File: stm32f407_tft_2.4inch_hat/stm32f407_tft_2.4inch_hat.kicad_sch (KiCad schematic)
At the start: 3 parts, among them P1 Conn_02x25_Row_Letter_First_S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, P2 Conn_02x25_Row_Letter_First_S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, U1 CR2013-MI2120

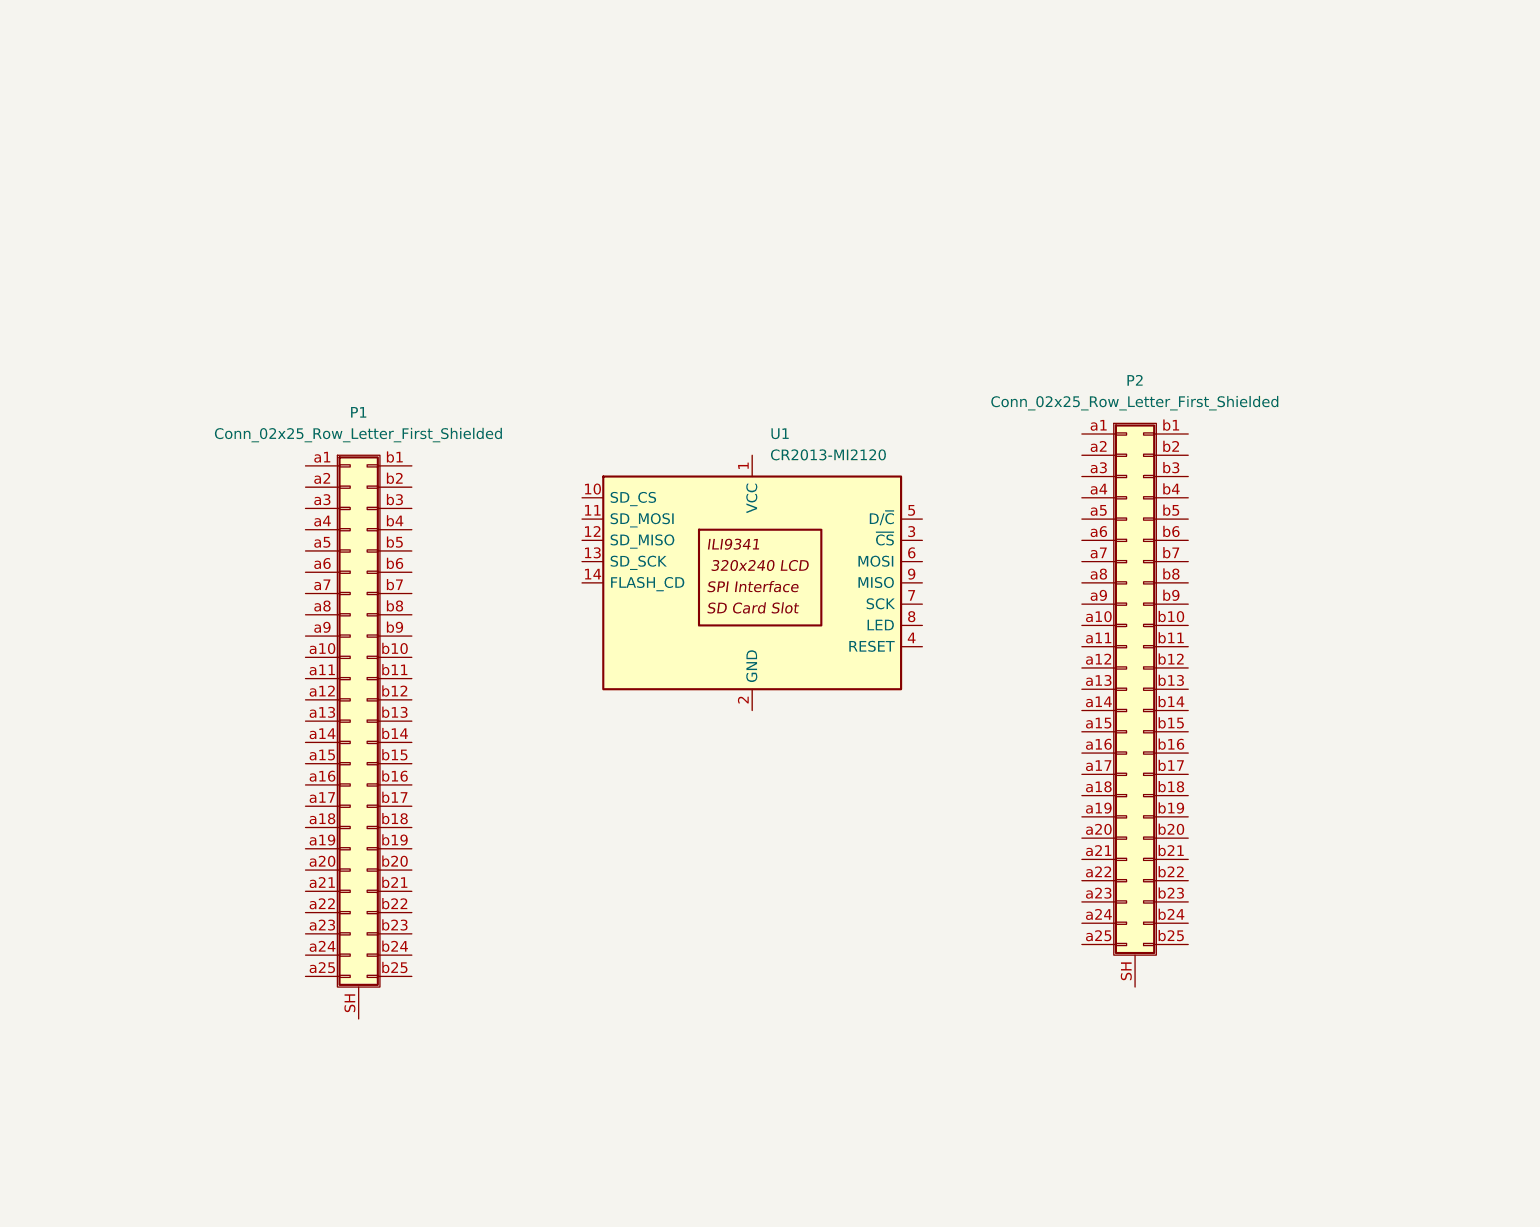
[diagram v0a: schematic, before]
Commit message: Add 3 connector for i2c & uart
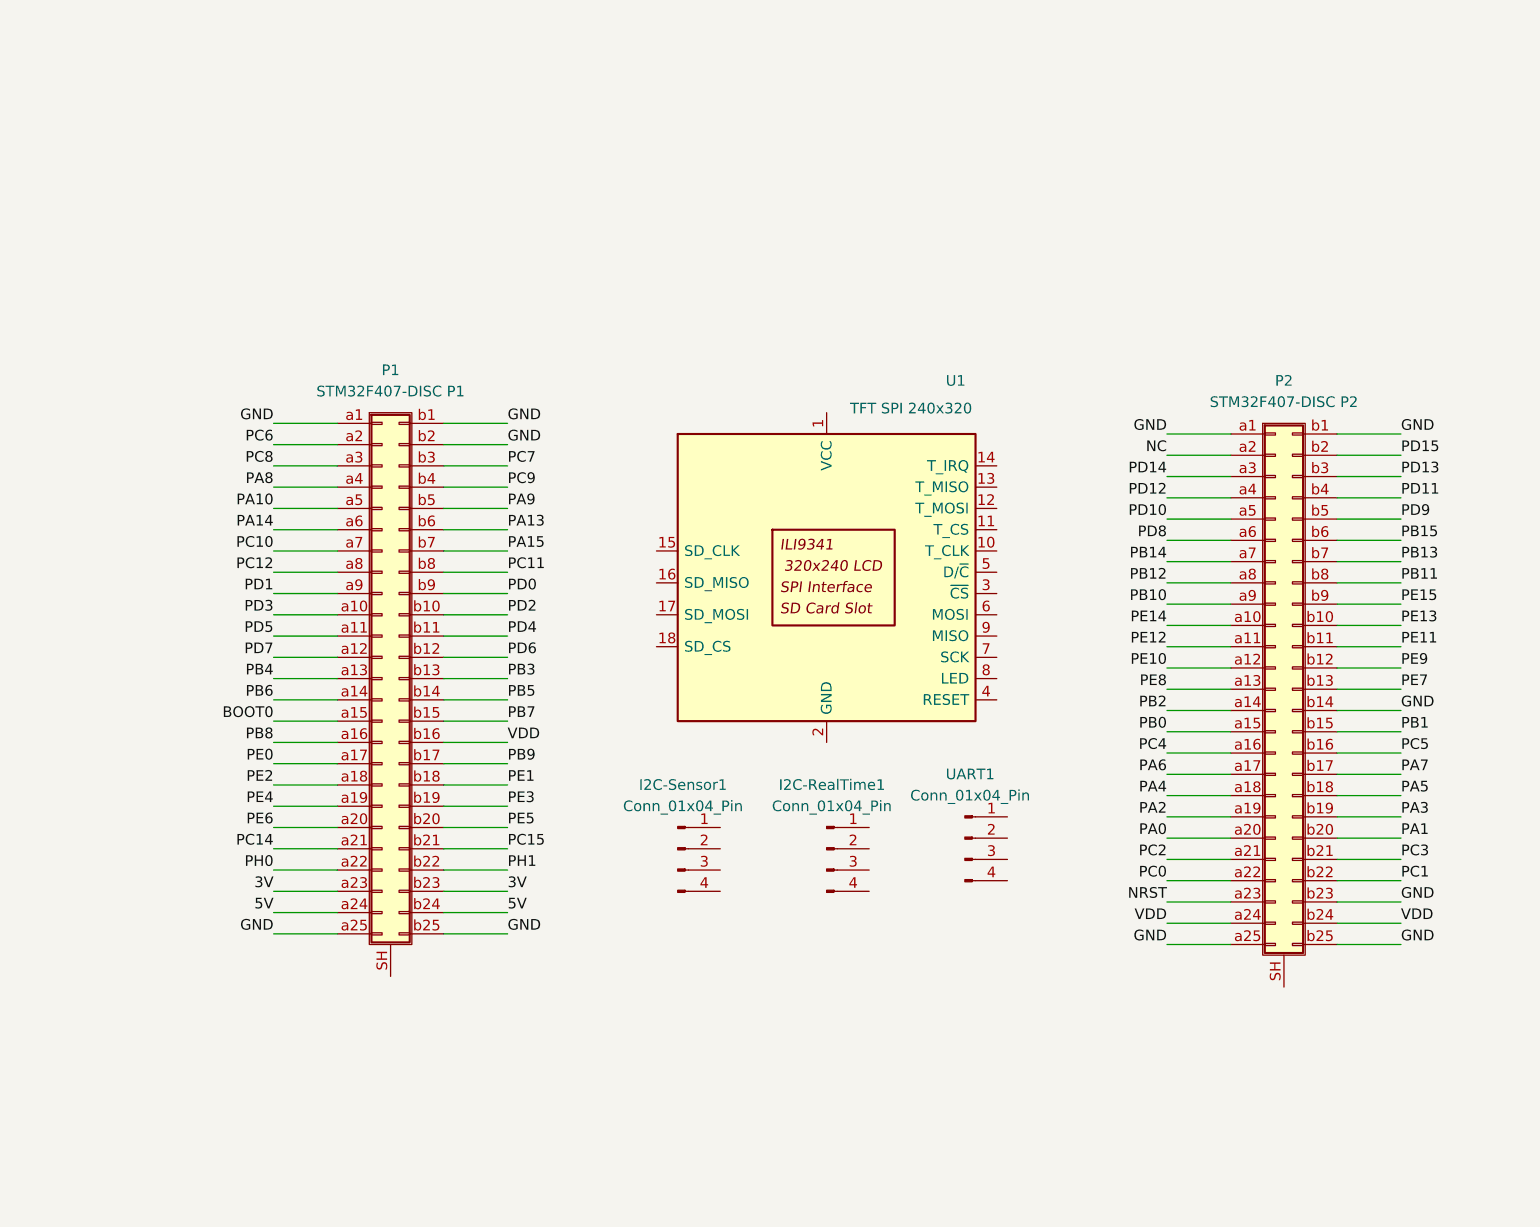
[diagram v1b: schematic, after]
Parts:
- added I2C-RealTime1, I2C-Sensor1, UART1: Conn_01x04_Pin, Connector_PinHeader_2.54mm:PinHeader_1x04_P2.54mm_Horizontal, symbol Connector:Conn_01x04_Pin
- P1: value Conn_02x25_Row_Letter_First_Shielded -> STM32F407-DISC P1; symbol Connector_Generic_Shielded:Conn_02x25_Row_Letter_First_Shielded -> stm32f407_tft_hat:Conn_Discovery_P1_2x25
- P2: value Conn_02x25_Row_Letter_First_Shielded -> STM32F407-DISC P2; symbol Connector_Generic_Shielded:Conn_02x25_Row_Letter_First_Shielded -> stm32f407_tft_hat:Conn_Discovery_P2_2x25
- U1: value CR2013-MI2120 -> TFT SPI 240x320
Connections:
- net GND: now reaches P1.a1 (GND)
- net GND: now also P1.a25 (GND), P1.b1 (GND), P1.b2 (5V), P1.b25 (GND), P2.a1 (GND), P2.a25 (GND), P2.b1 (GND), P2.b14 (PE9), P2.b23 (PD13), P2.b25 (GND)
- net PD3: now reaches P1.a10 (PB8)
- net PD5: now reaches P1.a11 (BOOT0)
- net PD7: now reaches P1.a12 (PB6)
- net PB4: now reaches P1.a13 (PB4)
- net PB6: now reaches P1.a14 (PD7)
- net BOOT0: now reaches P1.a15 (PD5)
- net PB8: now reaches P1.a16 (PD3)
- net PE0: now reaches P1.a17 (PD1)
- net PE2: now reaches P1.a18 (PC12)
- net PE4: now reaches P1.a19 (PC10)
- net PC6: now reaches P1.a2 (5V)
- net PE6: now reaches P1.a20 (PA14)
- net PC14: now reaches P1.a21 (PA10)
- net PH0: now reaches P1.a22 (PA8)
- net 3V: now reaches P1.a23 (PC8)
- net 3V: now also P1.b23 (PC7)
- net 5V: now reaches P1.a24 (PC6)
- net 5V: now also P1.b24 (GND)
- net PC8: now reaches P1.a3 (3V)
- net PA8: now reaches P1.a4 (PH0)
- net PA10: now reaches P1.a5 (PC14)
- net PA14: now reaches P1.a6 (PE6)
- net PC10: now reaches P1.a7 (PE4)
- net PC12: now reaches P1.a8 (PE2)
- net PD1: now reaches P1.a9 (PE0)
- net PD2: now reaches P1.b10 (VDD)
- net PD4: now reaches P1.b11 (PB7)
- net PD6: now reaches P1.b12 (PB5)
- net PB3: now reaches P1.b13 (PB3)
- net PB5: now reaches P1.b14 (PD6)
- net PB7: now reaches P1.b15 (PD4)
- net VDD: now reaches P1.b16 (PD2)
- net VDD: now also P2.a24 (NC), P2.b24 (PD15)
- net PB9: now reaches P1.b17 (PD0)
- net PE1: now reaches P1.b18 (PC11)
- net PE3: now reaches P1.b19 (PA15)
- net PE5: now reaches P1.b20 (PA13)
- net PC15: now reaches P1.b21 (PA9)
- net PH1: now reaches P1.b22 (PC9)
- net PC7: now reaches P1.b3 (3V)
- net PC9: now reaches P1.b4 (PH1)
- net PA9: now reaches P1.b5 (PC15)
- net PA13: now reaches P1.b6 (PE5)
- net PA15: now reaches P1.b7 (PE3)
- net PC11: now reaches P1.b8 (PE1)
- net PD0: now reaches P1.b9 (PB9)
- net PE14: now reaches P2.a10 (PC4)
- net PE12: now reaches P2.a11 (PB0)
- net PE10: now reaches P2.a12 (PB2)
- net PE8: now reaches P2.a13 (PE8)
- net PB2: now reaches P2.a14 (PE10)
- net PB0: now reaches P2.a15 (PE12)
- net PC4: now reaches P2.a16 (PE14)
- net PA6: now reaches P2.a17 (PB10)
- net PA4: now reaches P2.a18 (PB12)
- net PA2: now reaches P2.a19 (PB14)
- net NC: now reaches P2.a2 (VDD)
- net PA0: now reaches P2.a20 (PD8)
- net PC2: now reaches P2.a21 (PD10)
- net PC0: now reaches P2.a22 (PD12)
- net NRST: now reaches P2.a23 (PD14)
- net PD14: now reaches P2.a3 (NRST)
- net PD12: now reaches P2.a4 (PC0)
- net PD10: now reaches P2.a5 (PC2)
- net PD8: now reaches P2.a6 (PA0)
- net PB14: now reaches P2.a7 (PA2)
- net PB12: now reaches P2.a8 (PA4)
- net PB10: now reaches P2.a9 (PA6)
- net PE13: now reaches P2.b10 (PC5)
- net PE11: now reaches P2.b11 (PB1)
- net PE9: now reaches P2.b12 (GND)
- net PE7: now reaches P2.b13 (PE7)
- net PB1: now reaches P2.b15 (PE11)
- net PC5: now reaches P2.b16 (PE13)
- net PA7: now reaches P2.b17 (PE15)
- net PA5: now reaches P2.b18 (PB11)
- net PA3: now reaches P2.b19 (PB13)
- net PD15: now reaches P2.b2 (VDD)
- net PA1: now reaches P2.b20 (PB15)
- net PC3: now reaches P2.b21 (PD9)
- net PC1: now reaches P2.b22 (PD11)
- net PD13: now reaches P2.b3 (GND)
- net PD11: now reaches P2.b4 (PC1)
- net PD9: now reaches P2.b5 (PC3)
- net PB15: now reaches P2.b6 (PA1)
- net PB13: now reaches P2.b7 (PA3)
- net PB11: now reaches P2.b8 (PA5)
- net PE15: now reaches P2.b9 (PA7)
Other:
- moved on the sheet: P1, P2

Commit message: Update sch pin j1 & j2
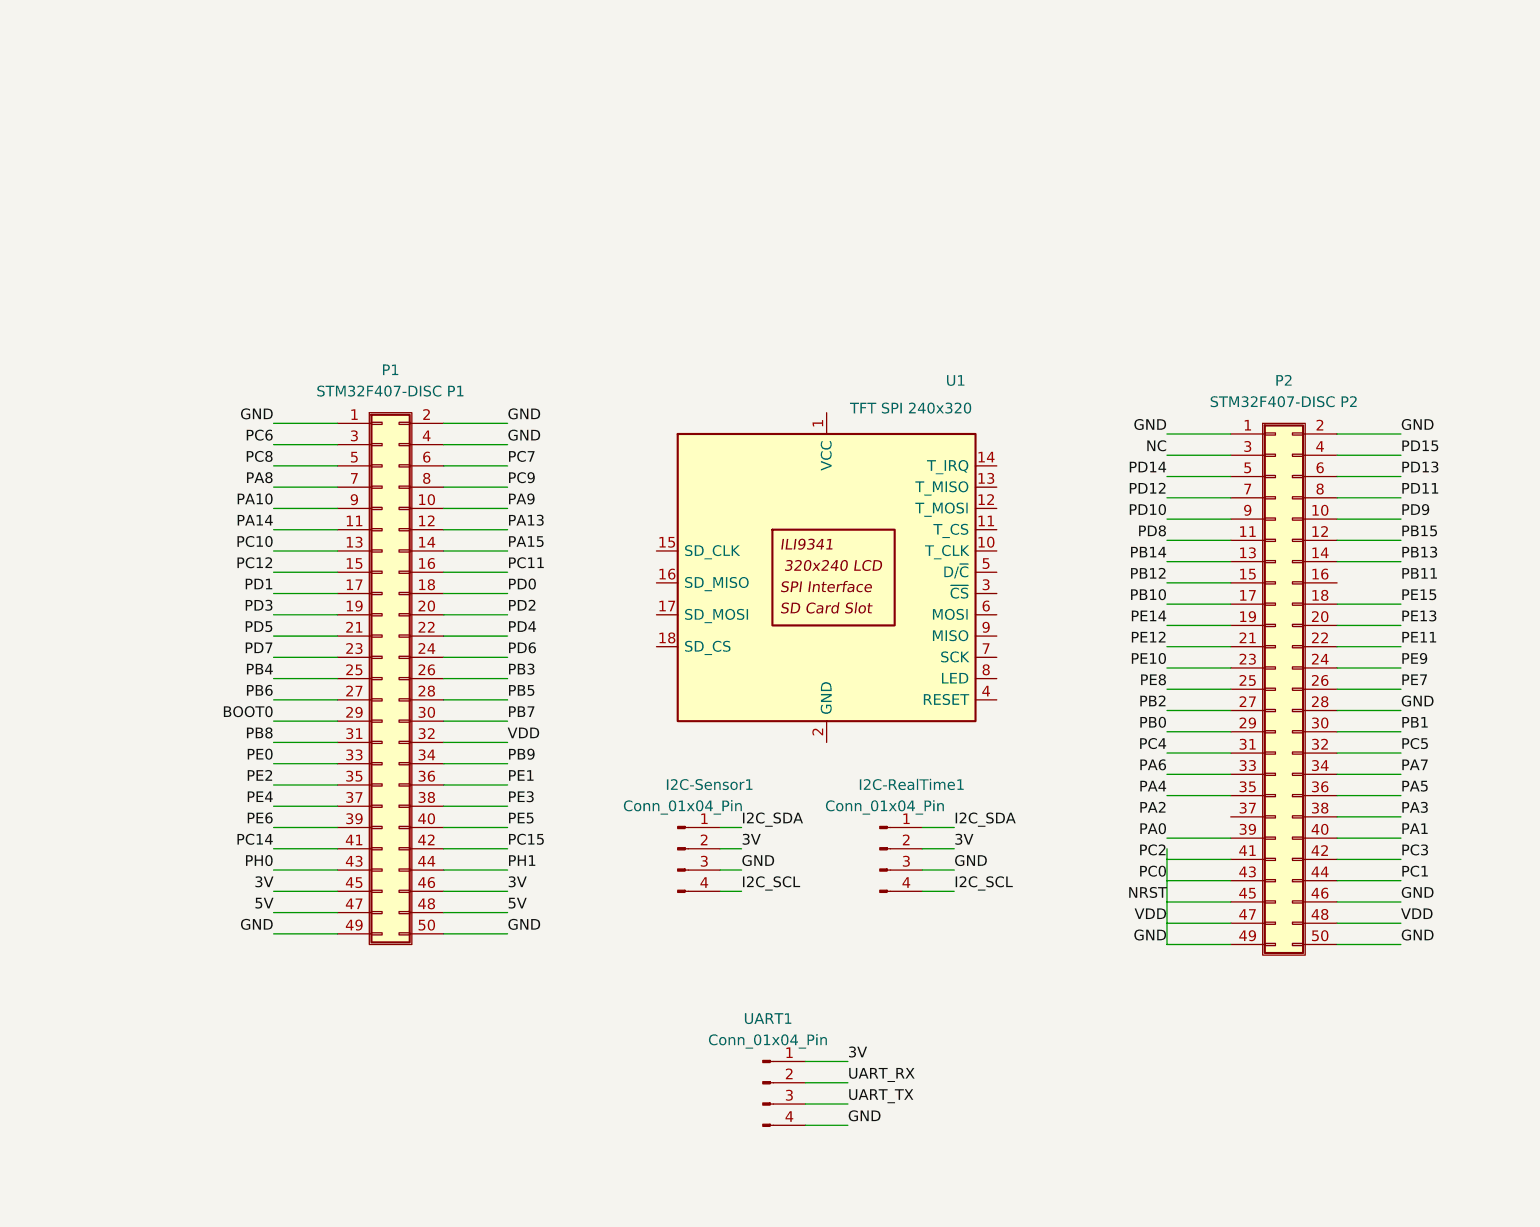
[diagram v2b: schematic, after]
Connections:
- net 3V: now also I2C-RealTime1.2 (Pin_2), I2C-Sensor1.2 (Pin_2), P1.45 (PC8), P1.46 (PC7), UART1.1 (Pin_1); no longer P1.a23 (PC8), P1.b23 (PC7)
- net 5V: now also P1.47 (PC6), P1.48 (GND); no longer P1.a24 (PC6), P1.b24 (GND)
- net BOOT0: now also P1.29 (PD5); no longer P1.a15 (PD5)
- net GND: now also I2C-RealTime1.3 (Pin_3), I2C-Sensor1.3 (Pin_3), P1.1 (GND), P1.2 (GND), P1.32 (PD2), P1.4 (5V), P1.49 (GND), P1.50 (GND), P2.1 (GND), P2.2 (GND), P2.28 (PE9), P2.41 (PD10), P2.43 (PD12), P2.45 (PD14), P2.46 (PD13), P2.47 (NC), P2.48 (PD15), P2.49 (GND), P2.50 (GND), UART1.4 (Pin_4); no longer P1.a1 (GND), P1.a25 (GND), P1.b1 (GND), P1.b2 (5V), P1.b25 (GND), P2.a1 (GND), P2.a25 (GND), P2.b1 (GND), P2.b14 (PE9), P2.b23 (PD13), P2.b25 (GND)
- net NC: now also P2.3 (VDD); no longer P2.a2 (VDD)
- net PA0: now also P2.39 (PD8); no longer P2.a20 (PD8)
- net PA1: now also P2.40 (PB15); no longer P2.b20 (PB15)
- net PA10: now also P1.9 (PC14); no longer P1.a5 (PC14)
- net PA13: now also P1.12 (PE5); no longer P1.b6 (PE5)
- net PA14: now also P1.11 (PE6); no longer P1.a6 (PE6)
- net PA15: now also P1.14 (PE3); no longer P1.b7 (PE3)
- net PA2: no longer P2.a19 (PB14)
- net PA3: now also P2.38 (PB13); no longer P2.b19 (PB13)
- net PA4: now also P2.35 (PB12); no longer P2.a18 (PB12)
- net PA5: now also P2.36 (PB11); no longer P2.b18 (PB11)
- net PA6: now also P2.33 (PB10); no longer P2.a17 (PB10)
- net PA7: now also P2.34 (PE15); no longer P2.b17 (PE15)
- net PA8: now also P1.7 (PH0); no longer P1.a4 (PH0)
- net PA9: now also P1.10 (PC15); no longer P1.b5 (PC15)
- net PB0: now also P2.29 (PE12); no longer P2.a15 (PE12)
- net PB1: now also P2.30 (PE11); no longer P2.b15 (PE11)
- net PB10: now also P2.17 (PA6); no longer P2.a9 (PA6)
- net PB11: no longer P2.b8 (PA5)
- net PB12: now also P2.15 (PA4); no longer P2.a8 (PA4)
- net PB13: now also P2.14 (PA3); no longer P2.b7 (PA3)
- net PB14: now also P2.13 (PA2); no longer P2.a7 (PA2)
- net PB15: now also P2.12 (PA1); no longer P2.b6 (PA1)
- net PB2: now also P2.27 (PE10); no longer P2.a14 (PE10)
- net PB3: now also P1.26 (PB3); no longer P1.b13 (PB3)
- net PB4: now also P1.25 (PB4); no longer P1.a13 (PB4)
- net PB5: now also P1.28 (PD6); no longer P1.b14 (PD6)
- net PB6: now also P1.27 (PD7); no longer P1.a14 (PD7)
- net PB7: now also P1.30 (PD4); no longer P1.b15 (PD4)
- net PB8: now also P1.31 (PD3); no longer P1.a16 (PD3)
- net PB9: now also P1.34 (PD0); no longer P1.b17 (PD0)
- net PC1: now also P2.44 (PD11); no longer P2.b22 (PD11)
- net PC10: now also P1.13 (PE4); no longer P1.a7 (PE4)
- net PC11: now also P1.16 (PE1); no longer P1.b8 (PE1)
- net PC12: now also P1.15 (PE2); no longer P1.a8 (PE2)
- net PC14: now also P1.41 (PA10); no longer P1.a21 (PA10)
- net PC15: now also P1.42 (PA9); no longer P1.b21 (PA9)
- net PC3: now also P2.42 (PD9); no longer P2.b21 (PD9)
- net PC4: now also P2.31 (PE14); no longer P2.a16 (PE14)
- net PC5: now also P2.32 (PE13); no longer P2.b16 (PE13)
- net PC6: now also P1.3 (5V); no longer P1.a2 (5V)
- net PC7: now also P1.6 (3V); no longer P1.b3 (3V)
- net PC8: now also P1.5 (3V); no longer P1.a3 (3V)
- net PC9: now also P1.8 (PH1); no longer P1.b4 (PH1)
- net PD0: now also P1.18 (PB9); no longer P1.b9 (PB9)
- net PD1: now also P1.17 (PE0); no longer P1.a9 (PE0)
- net PD10: now also P2.9 (PC2); no longer P2.a5 (PC2)
- net PD11: now also P2.8 (PC1); no longer P2.b4 (PC1)
- net PD12: now also P2.7 (PC0); no longer P2.a4 (PC0)
- net PD13: now also P2.6 (GND); no longer P2.b3 (GND)
- net PD14: now also P2.5 (NRST); no longer P2.a3 (NRST)
- net PD15: now also P2.4 (VDD); no longer P2.b2 (VDD)
- net PD2: now also P1.20 (VDD); no longer P1.b10 (VDD)
- net PD3: now also P1.19 (PB8); no longer P1.a10 (PB8)
- net PD4: now also P1.22 (PB7); no longer P1.b11 (PB7)
- net PD5: now also P1.21 (BOOT0); no longer P1.a11 (BOOT0)
- net PD6: now also P1.24 (PB5); no longer P1.b12 (PB5)
- net PD7: now also P1.23 (PB6); no longer P1.a12 (PB6)
- net PD8: now also P2.11 (PA0); no longer P2.a6 (PA0)
- net PD9: now also P2.10 (PC3); no longer P2.b5 (PC3)
- net PE0: now also P1.33 (PD1); no longer P1.a17 (PD1)
- net PE1: now also P1.36 (PC11); no longer P1.b18 (PC11)
- net PE10: now also P2.23 (PB2); no longer P2.a12 (PB2)
- net PE11: now also P2.22 (PB1); no longer P2.b11 (PB1)
- net PE12: now also P2.21 (PB0); no longer P2.a11 (PB0)
- net PE13: now also P2.20 (PC5); no longer P2.b10 (PC5)
- net PE14: now also P2.19 (PC4); no longer P2.a10 (PC4)
- net PE15: now also P2.18 (PA7); no longer P2.b9 (PA7)
- net PE2: now also P1.35 (PC12); no longer P1.a18 (PC12)
- net PE3: now also P1.38 (PA15); no longer P1.b19 (PA15)
- net PE4: now also P1.37 (PC10); no longer P1.a19 (PC10)
- net PE5: now also P1.40 (PA13); no longer P1.b20 (PA13)
- net PE6: now also P1.39 (PA14); no longer P1.a20 (PA14)
- net PE7: now also P2.26 (PE7); no longer P2.b13 (PE7)
- net PE8: now also P2.25 (PE8); no longer P2.a13 (PE8)
- net PE9: now also P2.24 (GND); no longer P2.b12 (GND)
- net PH0: now also P1.43 (PA8); no longer P1.a22 (PA8)
- net PH1: now also P1.44 (PC9); no longer P1.b22 (PC9)
- net UART_RX: now reaches UART1.2 (Pin_2)
- net UART_TX: now reaches UART1.3 (Pin_3)
- net I2C_SDA: now reaches I2C-Sensor1.1 (Pin_1)
- net I2C_SDA: now also I2C-RealTime1.1 (Pin_1)
- net I2C_SCL: now reaches I2C-Sensor1.4 (Pin_4)
- net I2C_SCL: now also I2C-RealTime1.4 (Pin_4)
- removed net NRST: P2.a23 (PD14)
- removed net PC0: P2.a22 (PD12)
- removed net PC2: P2.a21 (PD10)
- removed net VDD: P1.b16 (PD2), P2.a24 (NC), P2.b24 (PD15)
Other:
- moved on the sheet: I2C-RealTime1, UART1
